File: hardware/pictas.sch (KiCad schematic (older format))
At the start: 13 parts

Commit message: Work in progress PCB design
Signed-off-by: bigbass1997 <bigbass1997.website@gmail.com>
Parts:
- removed C? (x2): C, symbol Device:C
- removed J?: TTL to USB, symbol Connector_Generic:Conn_01x06
- removed J?: N64 Controller, symbol Connector_Generic:Conn_01x03
- removed R?: 10k, symbol Device:R
- removed U?: PIC18LF4550-IP-PinAligned, Package_DIP:DIP-40_W15.24mm, symbol MCU_Microchip_PIC18:PIC18LF4550-IP-PinAligned
- removed Y?: Crystal, symbol Device:Crystal
- added J1: NES_CNT1, Connector_PinHeader_2.54mm:PinHeader_1x07_P2.54mm_Vertical, symbol Connector_Generic:Conn_01x07
- added J2: NES_CNT2, Connector_PinHeader_2.54mm:PinHeader_1x07_P2.54mm_Vertical, symbol Connector_Generic:Conn_01x07
- added J4: N64_CNT2, Connector_PinHeader_2.54mm:PinHeader_1x03_P2.54mm_Vertical, symbol Connector_Generic:Conn_01x03
- added J5: N64_CNT3, Connector_PinHeader_2.54mm:PinHeader_1x03_P2.54mm_Vertical, symbol Connector_Generic:Conn_01x03
- added J6: N64_CNT4, Connector_PinHeader_2.54mm:PinHeader_1x03_P2.54mm_Vertical, symbol Connector_Generic:Conn_01x03
- added R1, R2, R3, R4: 10k, Resistor_THT:R_Axial_DIN0204_L3.6mm_D1.6mm_P5.08mm_Horizontal, symbol Device:R_Small
- J3: renamed from J?; value N64 Controller -> N64_CNT1; footprint (none) -> Connector_PinHeader_2.54mm:PinHeader_1x03_P2.54mm_Vertical
- J7: renamed from J?; value ICSProgrammer -> ICSP; footprint (none) -> Connector_PinHeader_2.54mm:PinHeader_1x05_P2.54mm_Vertical
- J8: renamed from J?; footprint (none) -> Connector_USB:USB_B_OST_USB-B1HSxx_Horizontal
- R5: renamed from R?; footprint (none) -> Resistor_THT:R_Axial_DIN0204_L3.6mm_D1.6mm_P5.08mm_Horizontal
- U1: renamed from U?; footprint (none) -> Package_DIP:DIP-40_W15.24mm
- U2: renamed from U?; footprint Package_SO:SOIC-8_5.23x5.23mm_P1.27mm -> Package_SO:SOIC-8_5.275x5.275mm_P1.27mm; symbol Memory_Flash:W25Q128JVS_PinAligned -> pictas-rescue:W25Q128JVS_PinAligned-Memory_Flash
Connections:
- net labels added: N64_DATA1, N64_DATA2, N64_DATA3, N64_DATA4, NES_5V, NES_CLK1, NES_CLK2, NES_D31, NES_D32, NES_D41, NES_D42, NES_DATA1, NES_DATA2, NES_LATCH, SPI1SCK, SPI1SDI, SPI1SDO, U1RX, U1TX, USB_5V, ~CS
- net labels removed: -->U1RX, -->USB_RX, 5V_HOST, <--U1TX, <--USB_TX, DATA, GND_HOST
- wire segments 81 -> 132
- no-connect marks 32 -> 20
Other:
- note removed: "N64 Port 1"
- note removed: "TTL to USB Adapter"
- moved on the sheet: J3, J7, J8, R5, U1

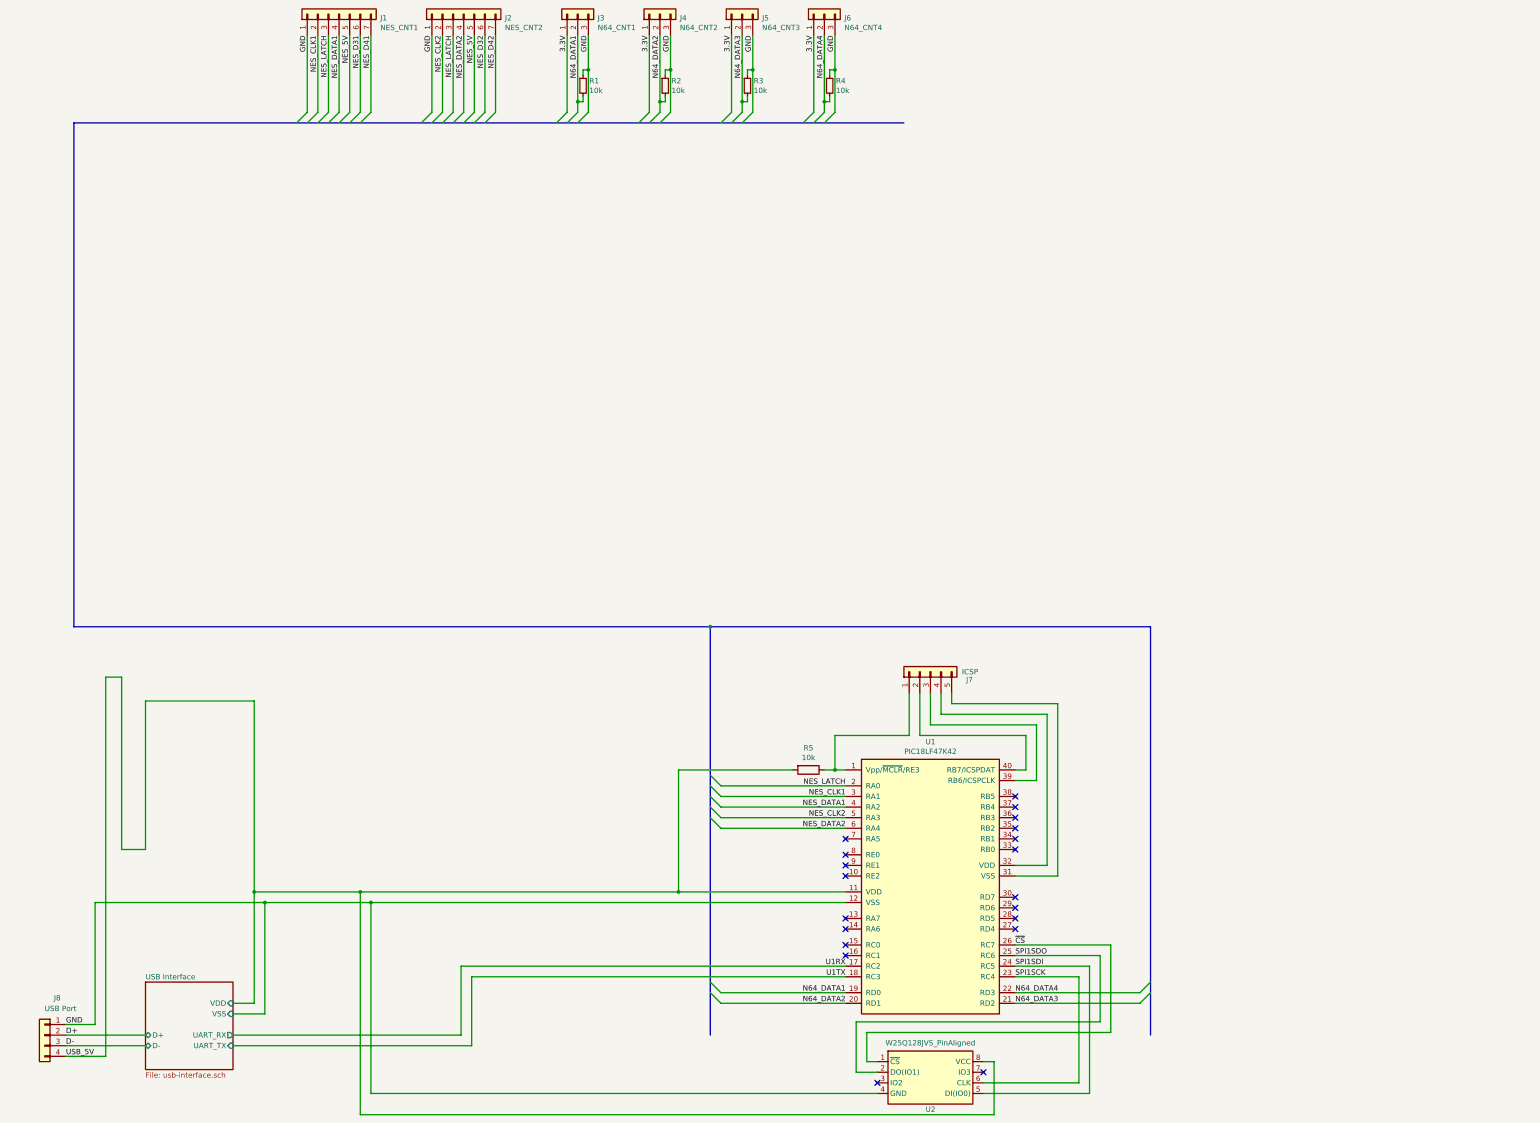
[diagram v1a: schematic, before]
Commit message: Redesigned PCB. Better controller placement and added visualization board connectors.
Signed-off-by: bigbass1997 <bigbass1997.website@gmail.com>
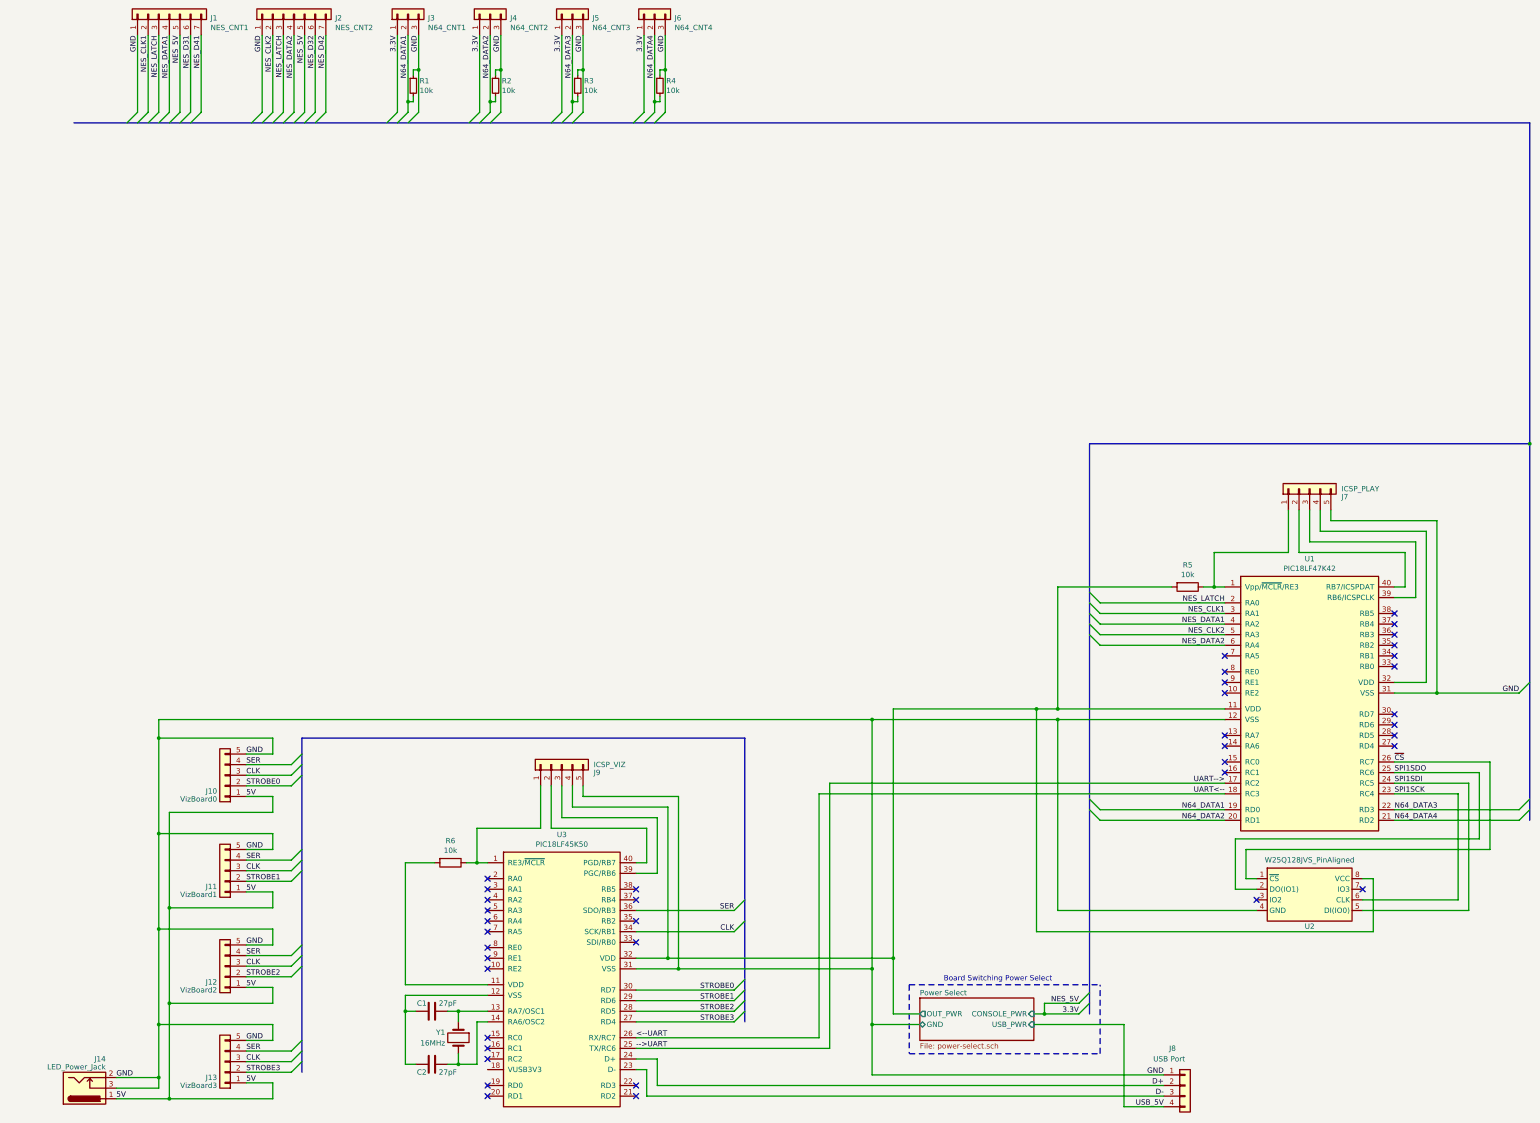
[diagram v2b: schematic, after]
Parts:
- added C1, C2: 27pF, Capacitor_THT:C_Disc_D3.0mm_W2.0mm_P2.50mm, symbol Device:C
- added J10: VizBoard0, Connector_PinHeader_2.54mm:PinHeader_1x05_P2.54mm_Horizontal, symbol Connector_Generic:Conn_01x05
- added J11: VizBoard1, Connector_PinHeader_2.54mm:PinHeader_1x05_P2.54mm_Horizontal, symbol Connector_Generic:Conn_01x05
- added J12: VizBoard2, Connector_PinHeader_2.54mm:PinHeader_1x05_P2.54mm_Horizontal, symbol Connector_Generic:Conn_01x05
- added J13: VizBoard3, Connector_PinHeader_2.54mm:PinHeader_1x05_P2.54mm_Horizontal, symbol Connector_Generic:Conn_01x05
- added J14: LED_Power_Jack, Connector_BarrelJack:BarrelJack_Horizontal, symbol Connector:Barrel_Jack_Switch
- added J9: ICSP_VIZ, Connector_PinHeader_2.54mm:PinHeader_1x05_P2.54mm_Vertical, symbol Connector_Generic:Conn_01x05
- added R6: 10k, Resistor_THT:R_Axial_DIN0204_L3.6mm_D1.6mm_P5.08mm_Horizontal, symbol Device:R
- added U3: PIC18LF45K50, Package_DIP:DIP-40_W15.24mm, symbol pictas:PIC18LF45K50
- added Y1: 16MHz, Crystal:Crystal_HC49-4H_Vertical, symbol Device:Crystal
- J7: value ICSP -> ICSP_PLAY
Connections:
- net NES_5V is gone; now on net 3.3V: J1.5 (Pin_5), J2.5 (Pin_5)
- net D+: now also U3.24 (D+)
- net D-: now also U3.23 (D-)
- net GND: now also J7.5 (Pin_5), U1.31 (VSS), J10.5 (Pin_5), J11.5 (Pin_5), J12.5 (Pin_5), J13.5 (Pin_5), J14.2, J14.3, J9.5 (Pin_5), U3.31 (VSS)
- net N64_DATA3: now also U1.22 (RD3); no longer U1.21 (RD2)
- net N64_DATA4: now also U1.21 (RD2); no longer U1.22 (RD3)
- net USB_5V: no longer R5.2, U1.11 (VDD), U2.8 (VCC)
- net U1RX renamed -->UART
- net -->UART: now also U3.25 (TX/RC6)
- net U1TX renamed <--UART
- net <--UART: now also U3.26 (RX/RC7)
- new net: C1.1, U3.13 (RA7/OSC1), Y1.1
- new net: C2.1, U3.14 (RA6/OSC2), Y1.2
- new net: C1.2, C2.2, U3.12 (VSS)
- new net: J9.1 (Pin_1), R6.1, U3.1 (RE3/~MCLR~)
- new net: R6.2, U3.11 (VDD)
- new net: J9.3 (Pin_3), U3.39 (PGC/RB6)
- new net: J9.2 (Pin_2), U3.40 (PGD/RB7)
- new net 5V: J10.1 (Pin_1), J11.1 (Pin_1), J12.1 (Pin_1), J13.1 (Pin_1), J14.1
- new net CLK: J10.3 (Pin_3), J11.3 (Pin_3), J12.3 (Pin_3), J13.3 (Pin_3), U3.34 (SCK/RB1)
- new net Power Select/OUT_PWR: J9.4 (Pin_4), R5.2, U1.11 (VDD), U2.8 (VCC), U3.32 (VDD)
- new net SER: J10.4 (Pin_4), J11.4 (Pin_4), J12.4 (Pin_4), J13.4 (Pin_4), U3.36 (SDO/RB3)
- new net STROBE0: J10.2 (Pin_2), U3.30 (RD7)
- new net STROBE1: J11.2 (Pin_2), U3.29 (RD6)
- new net STROBE2: J12.2 (Pin_2), U3.28 (RD5)
- new net STROBE3: J13.2 (Pin_2), U3.27 (RD4)
- no-connect marks 20 -> 40
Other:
- note added: "Board Switching Power Select"
- moved on the sheet: J1, J2, J3, J4, J5, J6, J7, J8, R1, R2, R3, R4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

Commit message: Updated schematic and prototype PCB design.
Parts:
- removed C1, C2: 27pF, Capacitor_THT:C_Disc_D3.0mm_W2.0mm_P2.50mm, symbol Device:C
- removed U3: PIC18LF45K50, Package_DIP:DIP-40_W15.24mm, symbol pictas:PIC18LF45K50
- removed Y1: 16MHz, Crystal:Crystal_HC49-4H_Vertical, symbol Device:Crystal
- added C1: 0.1uF, Capacitor_THT:C_Disc_D3.4mm_W2.1mm_P2.50mm, symbol Device:C_Small
- added U3: PIC18F27K42, Package_DIP:DIP-28_W7.62mm, symbol pictas:PIC18F27K42
- added U5: MCP2221A, Package_DIP:DIP-14_W7.62mm, symbol pictas:MCP2221A
- R6: value 10k -> 10K
- U1: symbol pictas:PIC18LF47K42 -> pictas-rescue:PIC18LF47K42-pictas
- U2: value W25Q128JVS_PinAligned -> W25Q128JVS
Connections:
- net CLK: now also U3.12 (RC1)
- net D+: now also U5.12 (D-)
- net D-: now also U5.13 (D+)
- net GND: now also C1.1, U3.19 (VSS), U5.14 (VSS)
- net Power Select/OUT_PWR: now also R6.2, U3.20 (VDD), U5.1 (VDD)
- net SER: now also U3.11 (RC0)
- net STROBE0: now also U3.4 (RA2)
- net STROBE1: now also U3.5 (RA3)
- net STROBE2: now also U3.6 (RA4)
- net STROBE3: now also U3.7 (RA5)
- net at J9.1 (Pin_1), R6.1: now also U3.1 (Vpp/~MCLR~/RE3)
- net at J9.3 (Pin_3): now also U3.27 (RB6/ICSPCLK)
- net at J9.2 (Pin_2): now also U3.28 (RB7/ICSPDAT)
- net -->UART renamed UART-->
- net UART-->: now also U3.25 (RB4)
- net <--UART renamed UART<--
- net UART<--: now also U3.26 (RB5)
- new net: U3.13 (RC2), U5.6 (UTx)
- new net: U3.14 (RC3), U5.5 (URx)
- new net: C1.2, U5.11 (VUSB)
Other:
- moved on the sheet: J10, J11, J12, J13, J14, J7, J8, J9, R5, R6, U1, U2

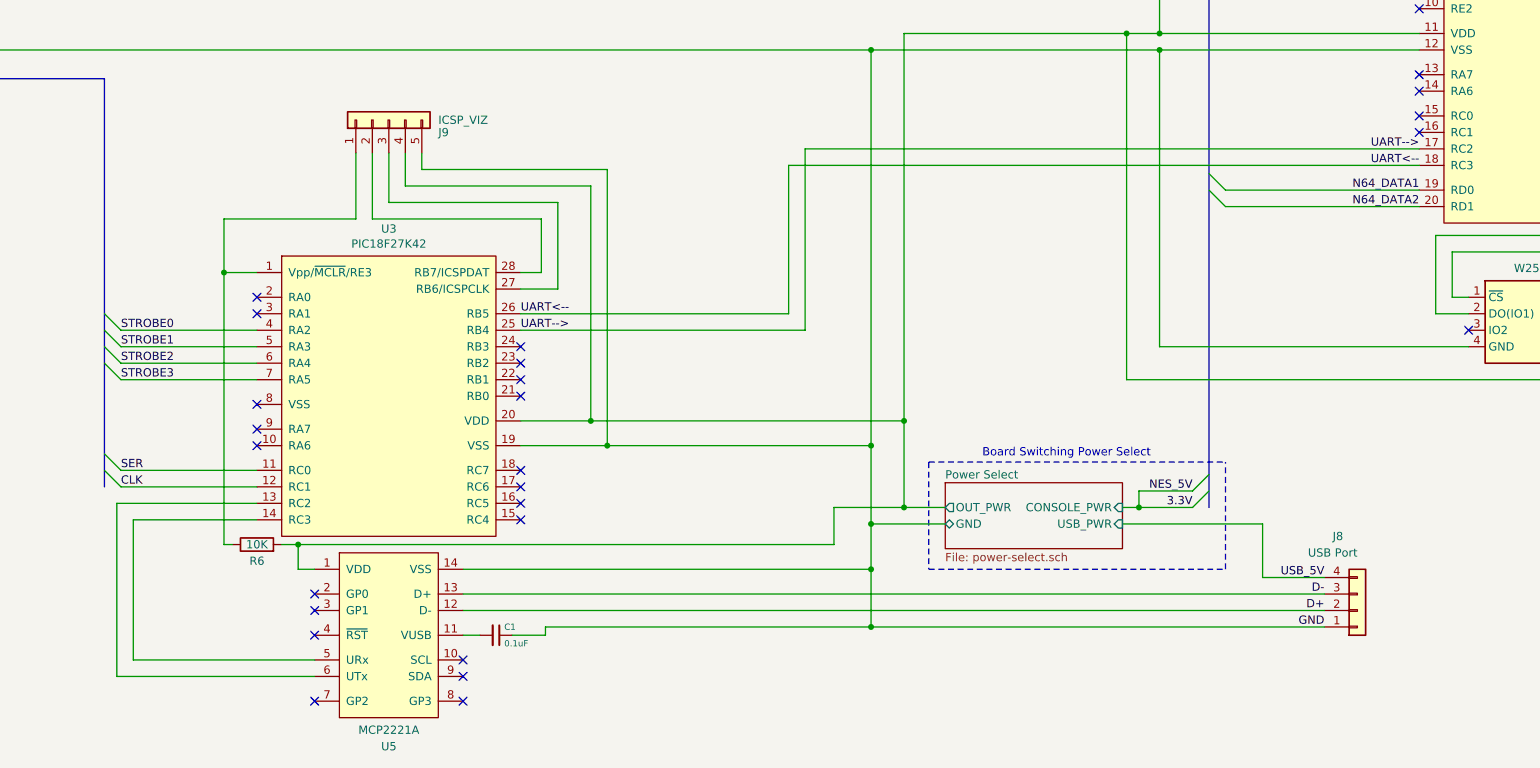
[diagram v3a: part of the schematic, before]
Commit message: Major overhaul to visual input display feature.
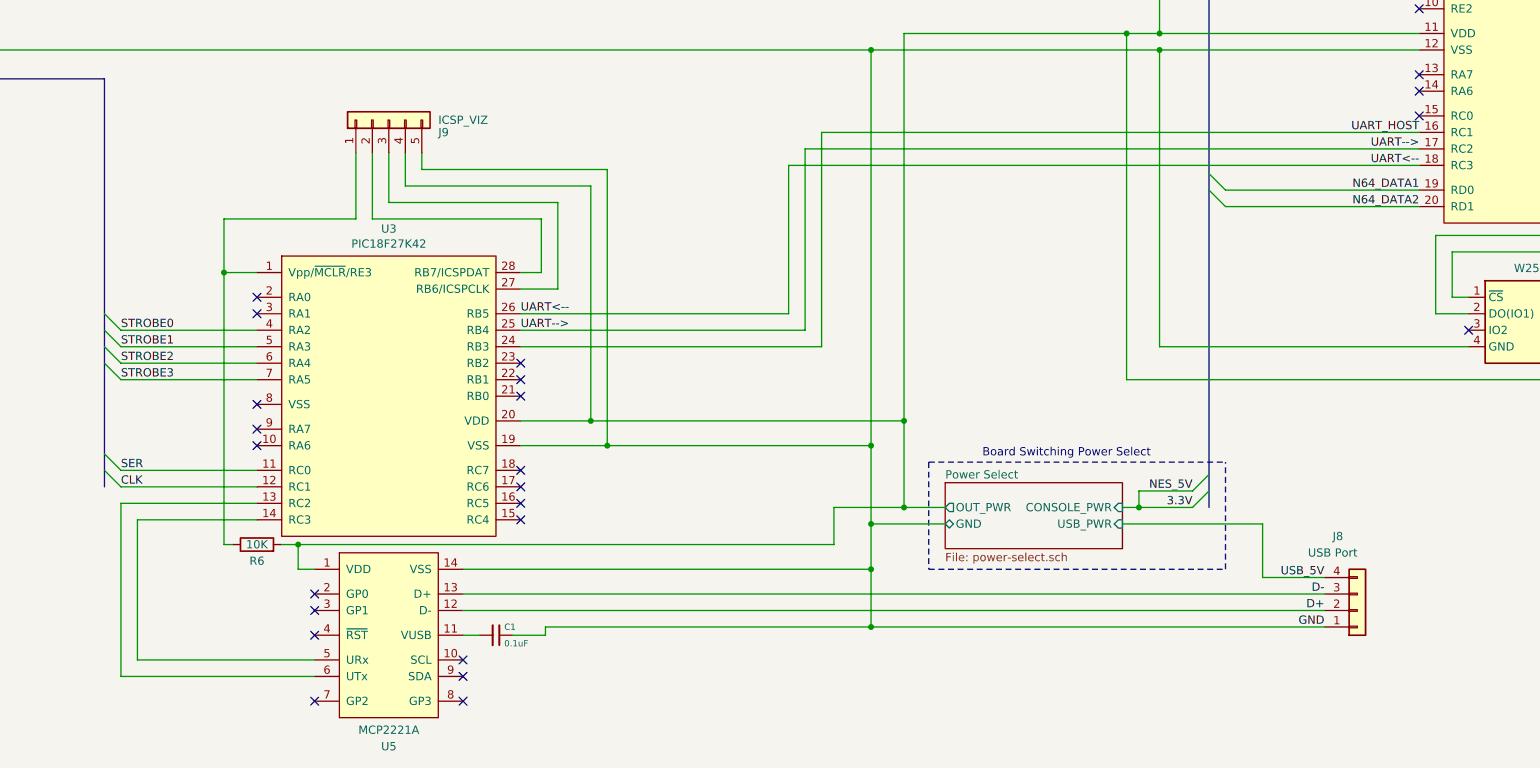
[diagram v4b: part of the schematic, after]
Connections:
- net UART_HOST: now reaches U1.16 (RC1)
- net UART_HOST: now also U3.24 (RB3)
- no-connect marks 40 -> 38
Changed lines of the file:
@@
 NoConn ~ 11950 6875
 NoConn ~ 11950 7025
-NoConn ~ 11950 7125
 NoConn ~ 13550 6875
 NoConn ~ 13550 6775
@@
 	6650 10125 8625 10125
 Wire Wire Line
-	5250 10325 4150 10325
-Wire Wire Line
-	4150 9475 4900 9475
-Wire Wire Line
-	5250 10425 4050 10425
-Wire Wire Line
-	4050 10425 4050 9375
-Wire Wire Line
-	4050 9375 4900 9375
-Wire Wire Line
-	4150 10325 4150 9475
+	5250 10325 4175 10325
+Wire Wire Line
+	4175 9475 4900 9475
+Wire Wire Line
+	5250 10425 4075 10425
+Wire Wire Line
+	4075 10425 4075 9375
+Wire Wire Line
+	4075 9375 4900 9375
+Wire Wire Line
+	4175 10325 4175 9475
 Wire Wire Line
 	6150 9775 8625 9775
@@
 NoConn ~ 4900 8225
 NoConn ~ 4900 8125
-NoConn ~ 6500 8425
 NoConn ~ 6500 8525
 NoConn ~ 4900 8775
@@
 $EndComp
 NoConn ~ 6500 9475
+Wire Wire Line
+	6500 8425 8325 8425
+Wire Wire Line
+	8325 8425 8325 7125
+Wire Wire Line
+	8325 7125 11950 7125
+Text Label 11950 7125 2    50   ~ 0
+UART_HOST
 Wire Bus Line
 	14825 4025 14825 7575
